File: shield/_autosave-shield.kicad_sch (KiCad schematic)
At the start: 9 parts, among them J1 Booster Pins, J2 Battery, J3 Conn_01x03_Female

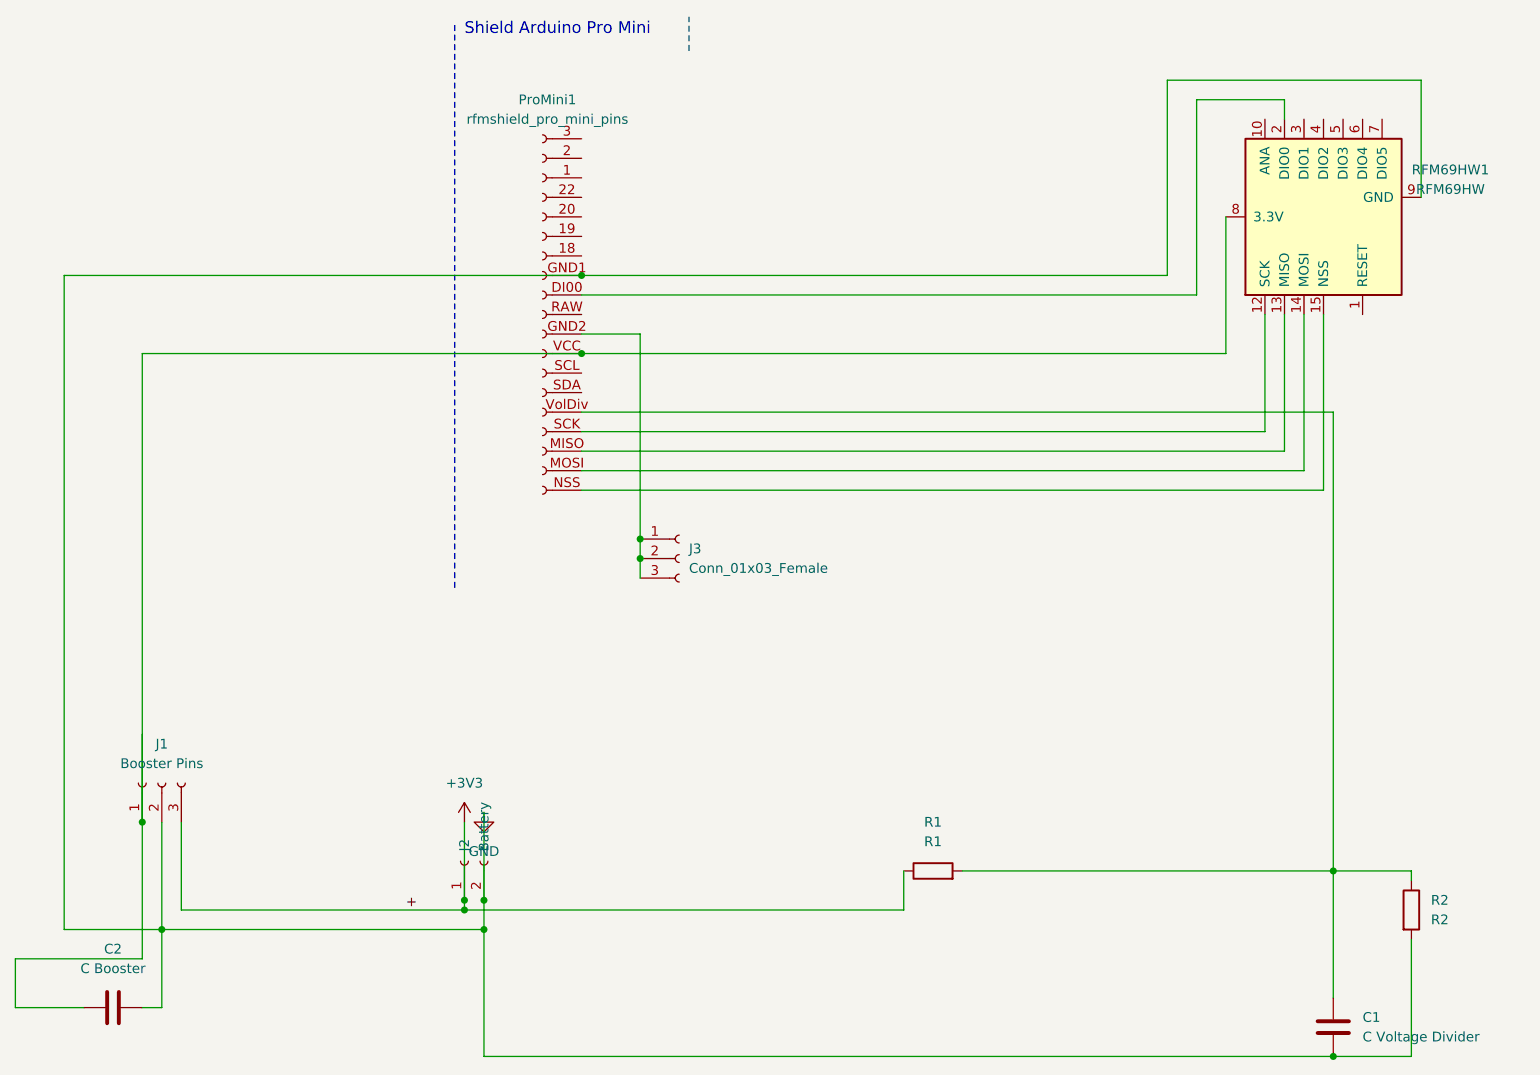
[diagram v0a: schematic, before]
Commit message: version v1alpha, sent to jclpcb
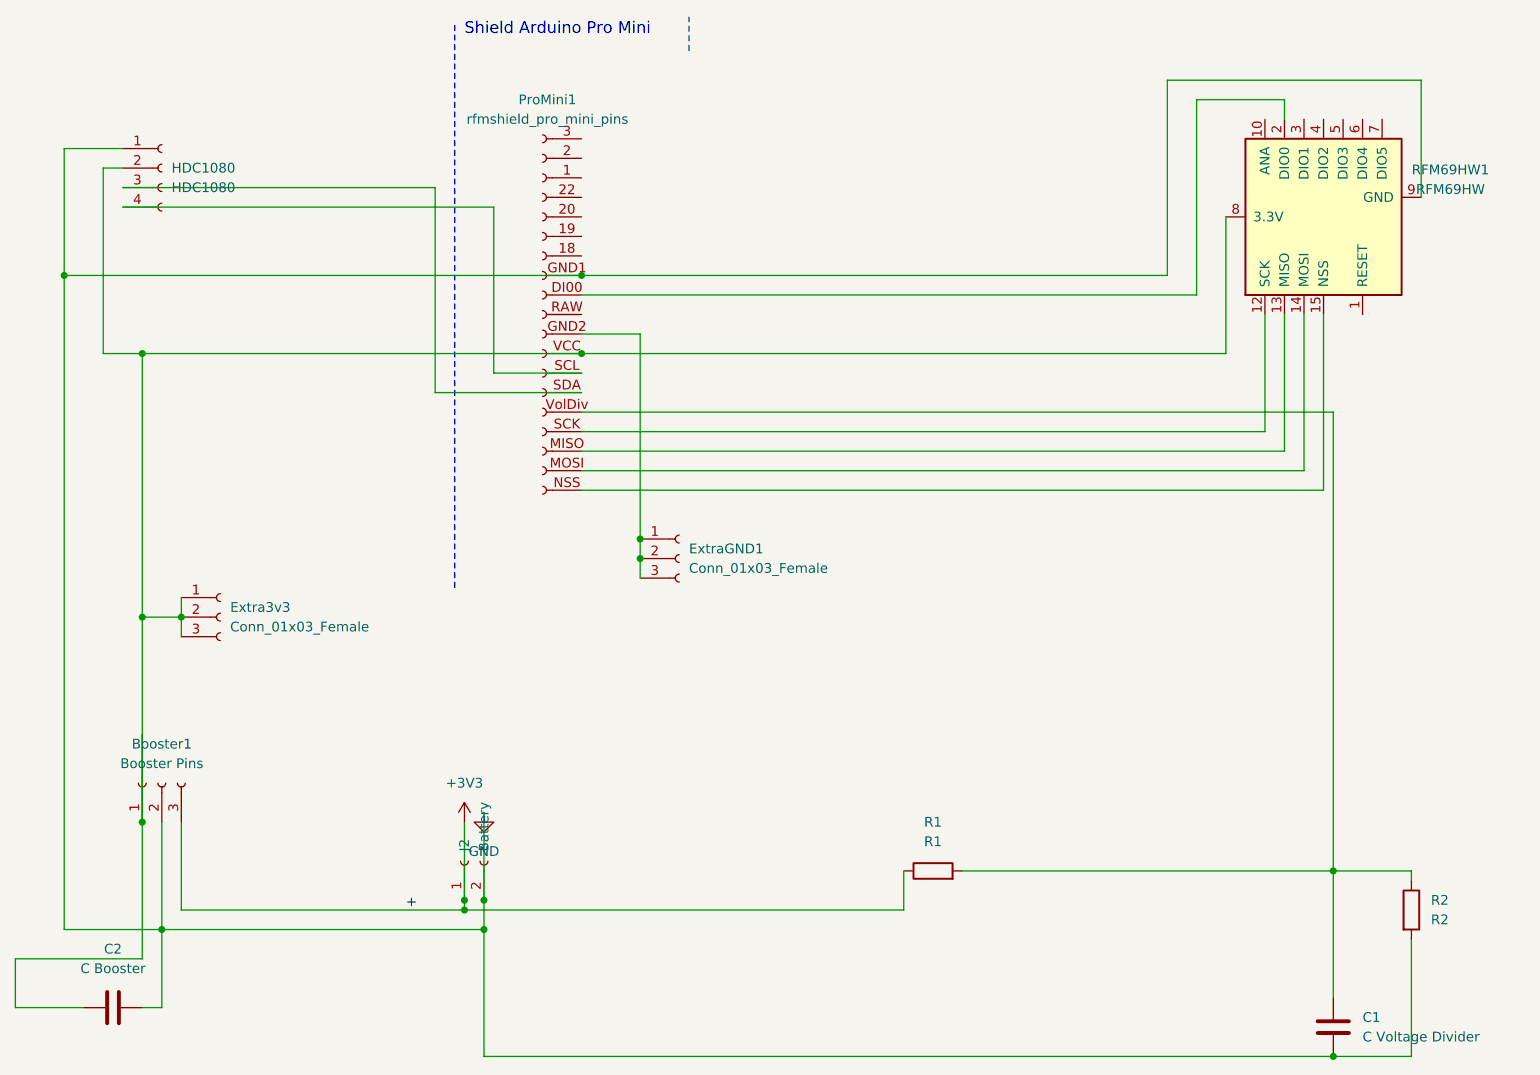
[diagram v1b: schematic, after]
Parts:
- added Extra3v3: Conn_01x03_Female, Connector_PinHeader_2.54mm:PinHeader_1x03_P2.54mm_Vertical, symbol Connector:Conn_01x03_Female
- added HDC1080: HDC1080, Connector_PinHeader_2.54mm:PinHeader_1x04_P2.54mm_Vertical, symbol Connector:Conn_01x04_Female
- renumbered J1 to Booster1, J3 to ExtraGND1
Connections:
- net GND: now also HDC1080.1 (Pin_1)
- net at ProMini1.SCL: now also HDC1080.4 (Pin_4)
- net at ProMini1.SDA: now also HDC1080.3 (Pin_3)
- net at Booster1.1 (Pin_1), C2.1, ProMini1.VCC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: now also Extra3v3.1 (Pin_1), Extra3v3.2 (Pin_2), Extra3v3.3 (Pin_3), HDC1080.2 (Pin_2)
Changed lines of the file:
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@@
   (junction (at 125.73 57.15) (diameter 0) (color 0 0 0 0)
   )
+  (junction (at 73.66 91.44) (diameter 0) (color 0 0 0 0)
+  )
   (junction (at 113.03 128.27) (diameter 0) (color 0 0 0 0)
   )
   (junction (at 223.52 148.59) (diameter 0) (color 0 0 0 0)
   )
+  (junction (at 68.58 57.15) (diameter 0) (color 0 0 0 0)
+  )
   (junction (at 71.12 132.08) (diameter 0) (color 0 0 0 0)
   )
+  (junction (at 68.58 91.44) (diameter 0) (color 0 0 0 0)
+  )
+  (junction (at 58.42 46.99) (diameter 0) (color 0 0 0 0)
+  )
   (junction (at 113.03 132.08) (diameter 0) (color 0 0 0 0)
   )
@@
     (stroke (width 0) (type default) (color 0 0 0 0))
   )
+  (wire (pts (xy 68.58 91.44) (xy 68.58 118.11))
+    (stroke (width 0) (type default) (color 255 0 0 1))
+  )
   (wire (pts (xy 233.68 133.35) (xy 233.68 148.59))
     (stroke (width 0) (type default) (color 0 0 0 0))
   )
+  (wire (pts (xy 66.04 33.02) (xy 63.5 33.02))
+    (stroke (width 0) (type default) (color 0 0 0 0))
+  )
+  (wire (pts (xy 114.3 59.69) (xy 125.73 59.69))
+    (stroke (width 0) (type default) (color 0 0 0 0))
+  )
   (wire (pts (xy 68.58 106.68) (xy 68.58 118.11))
     (stroke (width 0) (type default) (color 0 0 0 0))
@@
     (stroke (width 0) (type default) (color 0 0 0 0))
   )
-  (wire (pts (xy 68.58 57.15) (xy 68.58 118.11))
+  (wire (pts (xy 68.58 57.15) (xy 68.58 91.44))
     (stroke (width 0) (type default) (color 255 0 0 1))
   )
+  (wire (pts (xy 58.42 46.99) (xy 58.42 132.08))
+    (stroke (width 0) (type default) (color 0 0 0 0))
+  )
   (wire (pts (xy 125.73 69.85) (xy 217.17 69.85))
     (stroke (width 0) (type default) (color 0 0 0 0))
   )
   (wire (pts (xy 71.12 132.08) (xy 113.03 132.08))
+    (stroke (width 0) (type default) (color 0 0 0 0))
+  )
+  (wire (pts (xy 114.3 38.1) (xy 114.3 59.69))
     (stroke (width 0) (type default) (color 0 0 0 0))
   )
@@
     (stroke (width 0) (type default) (color 0 0 0 0))
   )
-  (wire (pts (xy 125.73 57.15) (xy 68.58 57.15))
+  (wire (pts (xy 68.58 57.15) (xy 125.73 57.15))
     (stroke (width 0) (type default) (color 0 0 0 0))
   )
@@
     (stroke (width 0) (type default) (color 0 0 0 0))
   )
+  (wire (pts (xy 68.58 91.44) (xy 73.66 91.44))
+    (stroke (width 0) (type default) (color 0 0 0 0))
+  )
   (wire (pts (xy 58.42 132.08) (xy 71.12 132.08))
+    (stroke (width 0) (type default) (color 0 0 0 0))
+  )
+  (wire (pts (xy 106.68 62.23) (xy 125.73 62.23))
     (stroke (width 0) (type default) (color 0 0 0 0))
   )
@@
     (stroke (width 0) (type default) (color 0 0 0 0))
   )
+  (wire (pts (xy 66.04 35.56) (xy 106.68 35.56))
+    (stroke (width 0) (type default) (color 0 0 0 0))
+  )
   (wire (pts (xy 133.35 54.61) (xy 133.35 81.28))
+    (stroke (width 0) (type default) (color 0 0 0 0))
+  )
+  (wire (pts (xy 66.04 30.48) (xy 58.42 30.48))
     (stroke (width 0) (type default) (color 0 0 0 0))
   )
@@
     (stroke (width 0) (type default) (color 0 0 0 0))
   )
-  (wire (pts (xy 58.42 46.99) (xy 58.42 132.08))
+  (wire (pts (xy 58.42 30.48) (xy 58.42 46.99))
+    (stroke (width 0) (type default) (color 0 0 0 0))
+  )
+  (wire (pts (xy 63.5 33.02) (xy 63.5 57.15))
     (stroke (width 0) (type default) (color 0 0 0 0))
   )
@@
     (stroke (width 0) (type default) (color 0 0 0 0))
   )
+  (wire (pts (xy 66.04 38.1) (xy 114.3 38.1))
+    (stroke (width 0) (type default) (color 0 0 0 0))
+  )
   (wire (pts (xy 113.03 132.08) (xy 113.03 148.59))
     (stroke (width 0) (type default) (color 0 0 0 0))
@@
     (stroke (width 0) (type default) (color 0 0 0 0))
   )
-  (wire (pts (xy 125.73 46.99) (xy 58.42 46.99))
+  (wire (pts (xy 58.42 46.99) (xy 125.73 46.99))
     (stroke (width 0) (type default) (color 0 0 0 0))
   )
@@
   )
   (wire (pts (xy 201.93 46.99) (xy 201.93 21.59))
+    (stroke (width 0) (type default) (color 0 0 0 0))
+  )
+  (wire (pts (xy 106.68 35.56) (xy 106.68 62.23))
+    (stroke (width 0) (type default) (color 0 0 0 0))
+  )
+  (wire (pts (xy 63.5 57.15) (xy 68.58 57.15))
     (stroke (width 0) (type default) (color 0 0 0 0))
   )
@@
     (stroke (width 0) (type default) (color 255 0 0 1))
   )
+  (wire (pts (xy 73.66 88.9) (xy 73.66 91.44))
+    (stroke (width 0) (type default) (color 0 0 0 0))
+  )
+  (wire (pts (xy 73.66 91.44) (xy 73.66 93.98))
+    (stroke (width 0) (type default) (color 0 0 0 0))
+  )
   (wire (pts (xy 125.73 46.99) (xy 201.93 46.99))
     (stroke (width 0) (type default) (color 0 0 0 0))
@@
     (effects (font (size 1.27 1.27)) (justify left bottom))
   )
+  (symbol (lib_id "Connector:Conn_01x03_Female") (at 78.74 91.44 0) (unit 1)
+    (in_bom yes) (on_board yes) (fields_autoplaced)
+    (property "Reference" "Extra3v3" (id 0) (at 80.01 90.1699 0)
+      (effects (font (size 1.27 1.27)) (justify left))
+    )
+    (property "Value" "Conn_01x03_Female" (id 1) (at 80.01 92.7099 0)
+      (effects (font (size 1.27 1.27)) (justify left))
+    )
+    (property "Footprint" "Connector_PinHeader_2.54mm:PinHeader_1x03_P2.54mm_Vertical" (id 2) (at 78.74 91.44 0)
+      (effects (font (size 1.27 1.27)) hide)
+    )
+    (property "Datasheet" "~" (id 3) (at 78.74 91.44 0)
+      (effects (font (size 1.27 1.27)) hide)
+    )
+    (pin "1")
+    (pin "2")
+    (pin "3")
+  )
   (symbol (lib_id "Device:C") (at 223.52 144.78 0) (unit 1)
     (in_bom yes) (on_board yes) (fields_autoplaced)
@@
   (symbol (lib_id "Connector:Conn_01x03_Female") (at 138.43 83.82 0) (unit 1)
     (in_bom yes) (on_board yes) (fields_autoplaced)
-    (property "Reference" "J3" (id 0) (at 139.7 82.5499 0)
+    (property "Reference" "ExtraGND1" (id 0) (at 139.7 82.5499 0)
       (effects (font (size 1.27 1.27)) (justify left))
     )
@@
     (pin "9")
   )
+  (symbol (lib_id "Connector:Conn_01x04_Female") (at 71.12 33.02 0) (unit 1)
+    (in_bom yes) (on_board yes) (fields_autoplaced)
+    (property "Reference" "HDC1080" (id 0) (at 72.39 33.0199 0)
+      (effects (font (size 1.27 1.27)) (justify left))
+    )
+    (property "Value" "HDC1080" (id 1) (at 72.39 35.5599 0)
+      (effects (font (size 1.27 1.27)) (justify left))
+    )
+    (property "Footprint" "Connector_PinHeader_2.54mm:PinHeader_1x04_P2.54mm_Vertical" (id 2) (at 71.12 33.02 0)
+      (effects (font (size 1.27 1.27)) hide)
+    )
+    (property "Datasheet" "~" (id 3) (at 71.12 33.02 0)
+      (effects (font (size 1.27 1.27)) hide)
+    )
+    (pin "1")
+    (pin "2")
+    (pin "3")
+    (pin "4")
+  )
   (symbol (lib_id "Connector:Conn_01x02_Female") (at 110.49 123.19 90) (unit 1)
     (in_bom yes) (on_board yes)
@@
   (symbol (lib_id "Connector:Conn_01x03_Female") (at 71.12 113.03 90) (unit 1)
     (in_bom yes) (on_board yes) (fields_autoplaced)
-    (property "Reference" "J1" (id 0) (at 71.12 107.95 90))
+    (property "Reference" "Booster1" (id 0) (at 71.12 107.95 90))
     (property "Value" "Booster Pins" (id 1) (at 71.12 110.49 90))
     (property "Footprint" "Connector_PinHeader_2.54mm:PinHeader_1x03_P2.54mm_Vertical" (id 2) (at 71.12 113.03 0)
@@
       (reference "#PWR0102") (unit 1) (value "GND") (footprint "")
     )
+    (path "/f022c12c-8ce1-4cb0-9f5f-a1e5ee7d0ba0"
+      (reference "Booster1") (unit 1) (value "Booster Pins") (footprint "Connector_PinHeader_2.54mm:PinHeader_1x03_P2.54mm_Vertical")
+    )
     (path "/386ab483-3160-4f1e-9c93-fbcb1e235786"
       (reference "C1") (unit 1) (value "C Voltage Divider") (footprint "Capacitor_THT:CP_Radial_D6.3mm_P2.50mm")
@@
       (reference "C2") (unit 1) (value "C Booster") (footprint "Capacitor_THT:CP_Radial_D6.3mm_P2.50mm")
     )
-    (path "/f022c12c-8ce1-4cb0-9f5f-a1e5ee7d0ba0"
-      (reference "J1") (unit 1) (value "Booster Pins") (footprint "Connector_PinHeader_2.54mm:PinHeader_1x03_P2.54mm_Vertical")
+    (path "/077985bd-c8a6-43b8-af30-1141a8334306"
+      (reference "Extra3v3") (unit 1) (value "Conn_01x03_Female") (footprint "Connector_PinHeader_2.54mm:PinHeader_1x03_P2.54mm_Vertical")
+    )
+    (path "/6ef5f8e0-5c2d-4349-9162-179c7c438d89"
+      (reference "ExtraGND1") (unit 1) (value "Conn_01x03_Female") (footprint "Connector_PinHeader_2.54mm:PinHeader_1x03_P2.54mm_Vertical")
+    )
+    (path "/b16db6aa-eff9-4560-94eb-8f1df0edf71a"
+      (reference "HDC1080") (unit 1) (value "HDC1080") (footprint "Connector_PinHeader_2.54mm:PinHeader_1x04_P2.54mm_Vertical")
     )
     (path "/b8790514-1424-44a6-b36e-2e7680815de1"
       (reference "J2") (unit 1) (value "Battery") (footprint "Connector_PinHeader_2.54mm:PinHeader_1x02_P2.54mm_Vertical")
     )
-    (path "/6ef5f8e0-5c2d-4349-9162-179c7c438d89"
-      (reference "J3") (unit 1) (value "Conn_01x03_Female") (footprint "Connector_PinHeader_2.54mm:PinHeader_1x03_P2.54mm_Vertical")
-    )
     (path "/a08c2c81-3e22-4b74-ac3d-76da4486ca80"
